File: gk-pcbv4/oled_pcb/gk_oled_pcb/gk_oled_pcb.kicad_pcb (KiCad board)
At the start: 4 copper layers, 50.7 x 52 mm, 48 parts, among them J2 Conn_01x01, J3 Conn_01x01, J4 Conn_01x06, J5 Conn_01x01, U1 TCA9546APW

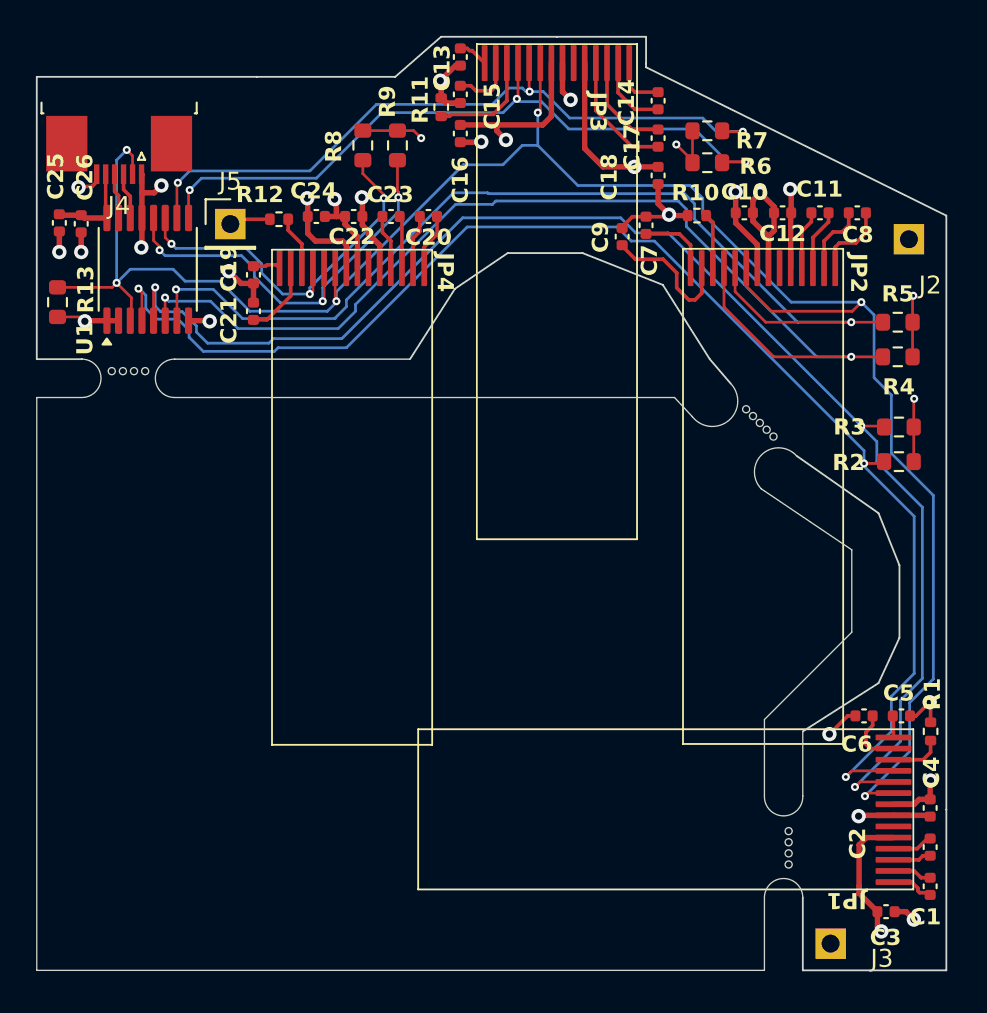
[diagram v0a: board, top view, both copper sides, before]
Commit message: nudge l + r oleds back a bit so they don't overlap with the down one when soldering
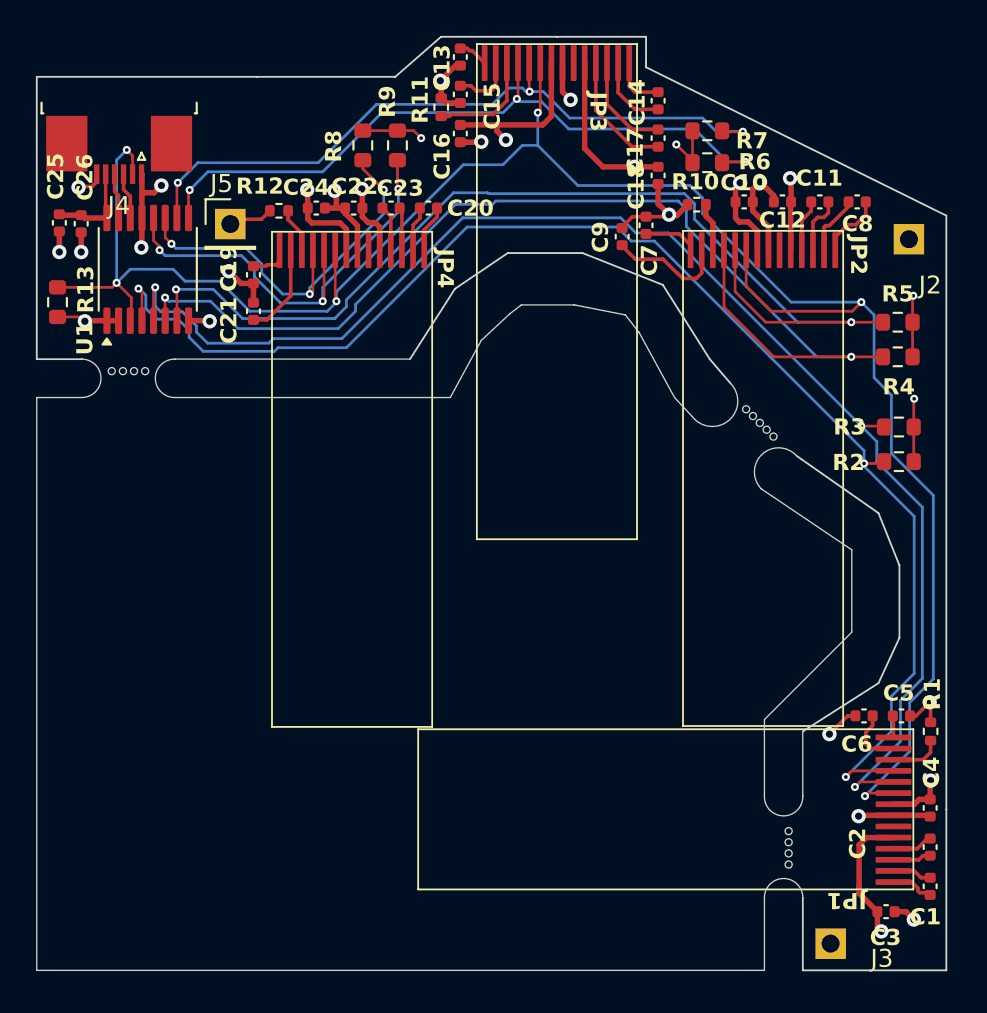
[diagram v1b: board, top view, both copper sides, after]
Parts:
- moved JP2 1.00 mm to (135.0, 74.8)
- moved JP4 1.00 mm to (112.1, 74.8)
- moved C10 0.61 mm to (133.9, 72.1)
- moved C11 0.61 mm to (138.1, 72.1)
- moved C12 0.61 mm to (136.1, 72.1)
- moved C8 0.61 mm to (140.2, 72.1)
- moved R10 0.61 mm to (131.3, 72.3)
- moved C20 0.47 mm to (116.3, 72.5)
- moved C22 0.47 mm to (112.2, 72.5)
- moved C23 0.47 mm to (114.2, 72.5)
- moved C24 0.47 mm to (110.1, 72.5)
- moved R12 0.47 mm to (108.0, 72.6)
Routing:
- net Net-(JP2-VCOMH): track 7.75 -> 5.62 mm
- net GND: track 53.1 -> 51.1 mm
- net Net-(JP2-VPP): track 4.03 -> 2.74 mm
- net VCC: track 63.5 -> 62.3 mm
- net Net-(JP2-C2P): track 4.33 -> 3.67 mm
- net Net-(JP4-VPP): track 1.57 -> 2.19 mm
- net Net-(JP2-C2N): track 3.95 -> 3.38 mm
- net Net-(JP4-IREF): track 3.04 -> 2.51 mm
- net Net-(JP4-C2P): track 3.18 -> 2.65 mm
- net Net-(JP4-C2N): track 3.04 -> 2.51 mm
- net Net-(JP4-C1P): track 2.93 -> 2.40 mm
- net Net-(JP4-C1N): track 3.07 -> 2.54 mm
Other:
- outline, holes or cut-outs redrawn
